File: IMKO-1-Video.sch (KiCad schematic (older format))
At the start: 5 parts, among them U18 82S129, U19 74LS244, U20 74LS244, U26 74LS374

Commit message: Caps, VID lines
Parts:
- added C15, C16: 150nF, symbol C
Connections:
- wire segments 79 -> 80
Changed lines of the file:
@@
-EESchema Schematic File Version 2  date Tue 09 Oct 2012 10:55:53 PM EEST
+EESchema Schematic File Version 2  date Tue 09 Oct 2012 11:59:32 PM EEST
 LIBS:power
 LIBS:device
@@
 LIBS:valves
 LIBS:o_memory
+LIBS:IMKO-1-Video-cache
 EELAYER 27 0
 EELAYER END
@@
 	3200 7100 3500 7100
 Wire Wire Line
-	3200 7200 3900 7200
-Wire Wire Line
-	3900 7200 4450 7200
+	3200 7200 4450 7200
 Wire Wire Line
 	3200 7300 3500 7300
@@
 V.D4
 $Comp
-L GND #PWR?
+L GND #PWR07
 U 1 1 50747FE3
 P 4000 4600
-F 0 "#PWR?" H 4000 4600 30  0001 C CNN
+F 0 "#PWR07" H 4000 4600 30  0001 C CNN
 F 1 "GND" H 4000 4530 30  0001 C CNN
 	1    4000 4600
@@
 	4050 4250 4000 4250
 Wire Wire Line
-	4000 4250 4000 4450
-Wire Wire Line
-	4000 4450 4000 4550
-Wire Wire Line
-	4000 4550 4000 4600
+	4000 4250 4000 4600
 Wire Wire Line
 	4050 4450 4000 4450
@@
 Text Label 3800 4150 0    60   ~ 0
 V.D6
+$Comp
+L C C15
+U 1 1 50748F6B
+P 6200 6600
+F 0 "C15" H 6250 6700 50  0000 L CNN
+F 1 "150nF" H 6250 6500 50  0000 L CNN
+	1    6200 6600
+	1    0    0    -1
+$EndComp
+$Comp
+L GND #PWR08
+U 1 1 50748F84
+P 6200 6850
+F 0 "#PWR08" H 6200 6850 30  0001 C CNN
+F 1 "GND" H 6200 6780 30  0001 C CNN
+	1    6200 6850
+	1    0    0    -1
+$EndComp
+$Comp
+L VCC #PWR09
+U 1 1 50748F8A
+P 6200 6350
+F 0 "#PWR09" H 6200 6450 30  0001 C CNN
+F 1 "VCC" H 6200 6450 30  0000 C CNN
+	1    6200 6350
+	1    0    0    -1
+$EndComp
+Wire Wire Line
+	6200 6350 6200 6400
+Wire Wire Line
+	6200 6800 6200 6850
+$Comp
+L C C16
+U 1 1 50749031
+P 5450 4600
+F 0 "C16" H 5500 4700 50  0000 L CNN
+F 1 "150nF" H 5500 4500 50  0000 L CNN
+	1    5450 4600
+	1    0    0    -1
+$EndComp
+$Comp
+L GND #PWR010
+U 1 1 50749037
+P 5450 4850
+F 0 "#PWR010" H 5450 4850 30  0001 C CNN
+F 1 "GND" H 5450 4780 30  0001 C CNN
+	1    5450 4850
+	1    0    0    -1
+$EndComp
+$Comp
+L VCC #PWR011
+U 1 1 5074903D
+P 5450 4350
+F 0 "#PWR011" H 5450 4450 30  0001 C CNN
+F 1 "VCC" H 5450 4450 30  0000 C CNN
+	1    5450 4350
+	1    0    0    -1
+$EndComp
+Wire Wire Line
+	5450 4350 5450 4400
+Wire Wire Line
+	5450 4800 5450 4850
 $EndSCHEMATC

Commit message: Added U25
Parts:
- added U25: 74LS00, symbol 74LS00
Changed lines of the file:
@@
-EESchema Schematic File Version 2  date Tue 09 Oct 2012 11:59:32 PM EEST
+EESchema Schematic File Version 2  date Wed 10 Oct 2012 12:46:06 AM EEST
 LIBS:power
 LIBS:device
@@
 Wire Wire Line
 	5450 4800 5450 4850
+$Comp
+L 74LS00 U25
+U 1 1 50749ACA
+P 7800 3450
+F 0 "U25" H 7800 3500 60  0000 C CNN
+F 1 "74LS00" H 7800 3350 60  0000 C CNN
+	1    7800 3450
+	1    0    0    -1
+$EndComp
+$Comp
+L 74LS00 U25
+U 2 1 50749AF2
+P 7800 3950
+F 0 "U25" H 7800 4000 60  0000 C CNN
+F 1 "74LS00" H 7800 3850 60  0000 C CNN
+	2    7800 3950
+	1    0    0    -1
+$EndComp
+$Comp
+L 74LS00 U25
+U 3 1 50749B0E
+P 7800 4450
+F 0 "U25" H 7800 4500 60  0000 C CNN
+F 1 "74LS00" H 7800 4350 60  0000 C CNN
+	3    7800 4450
+	1    0    0    -1
+$EndComp
+$Comp
+L 74LS00 U25
+U 4 1 50749B27
+P 7800 4950
+F 0 "U25" H 7800 5000 60  0000 C CNN
+F 1 "74LS00" H 7800 4850 60  0000 C CNN
+	4    7800 4950
+	1    0    0    -1
+$EndComp
 $EndSCHEMATC

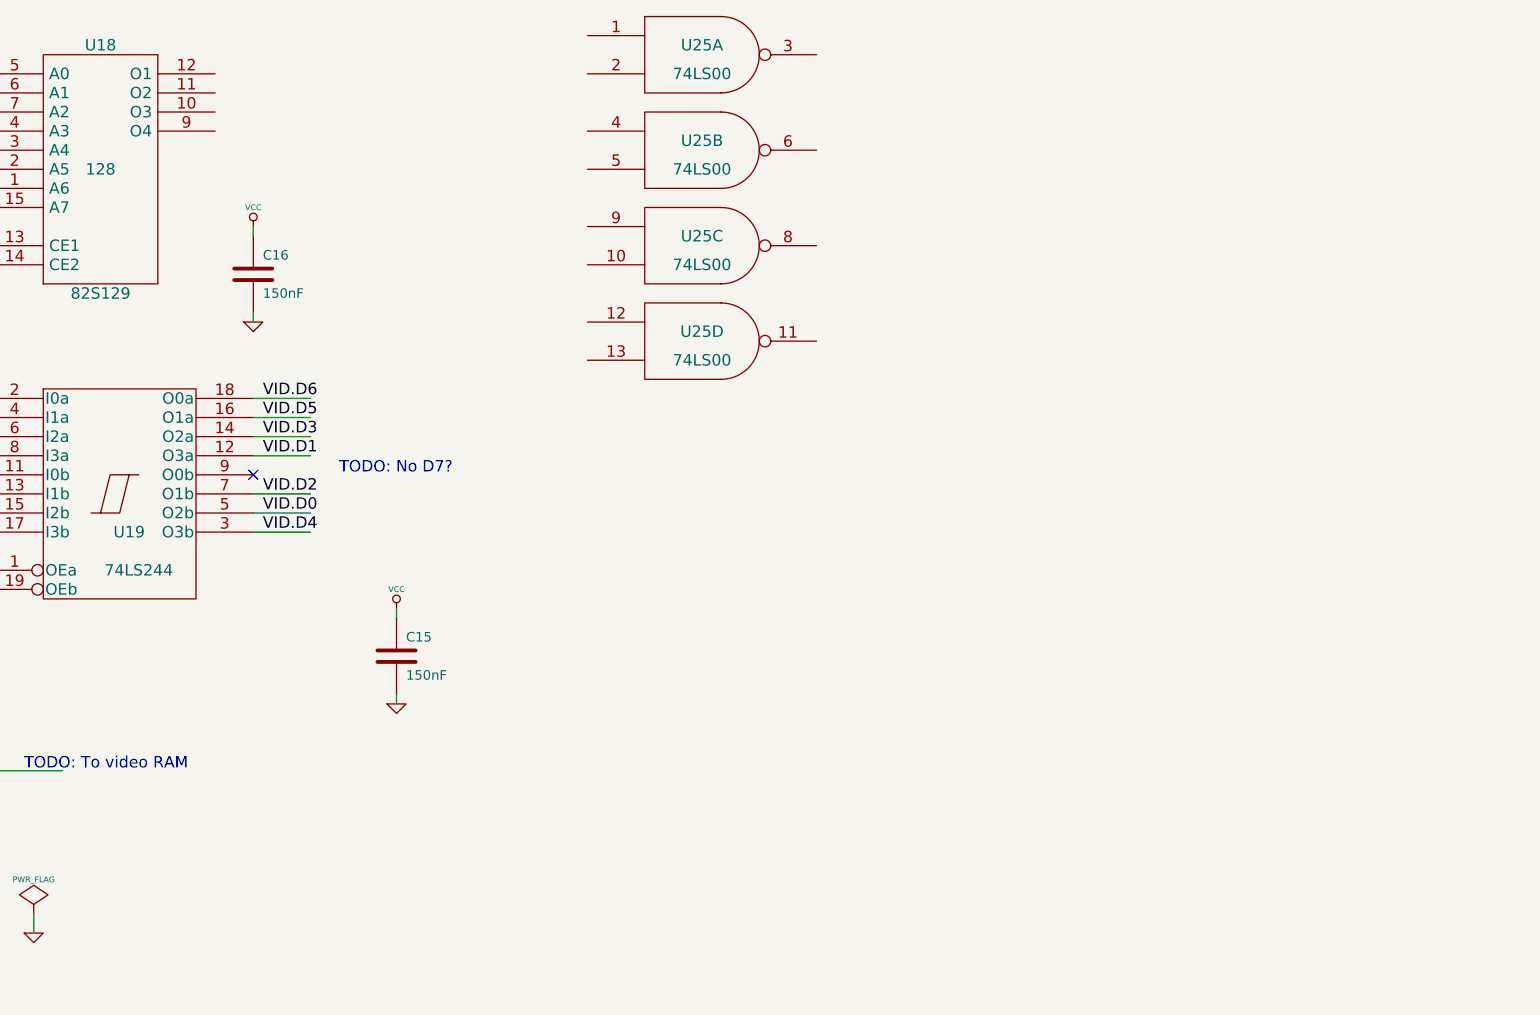
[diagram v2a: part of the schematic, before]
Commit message: Added U23, U24. Fixed caps lib
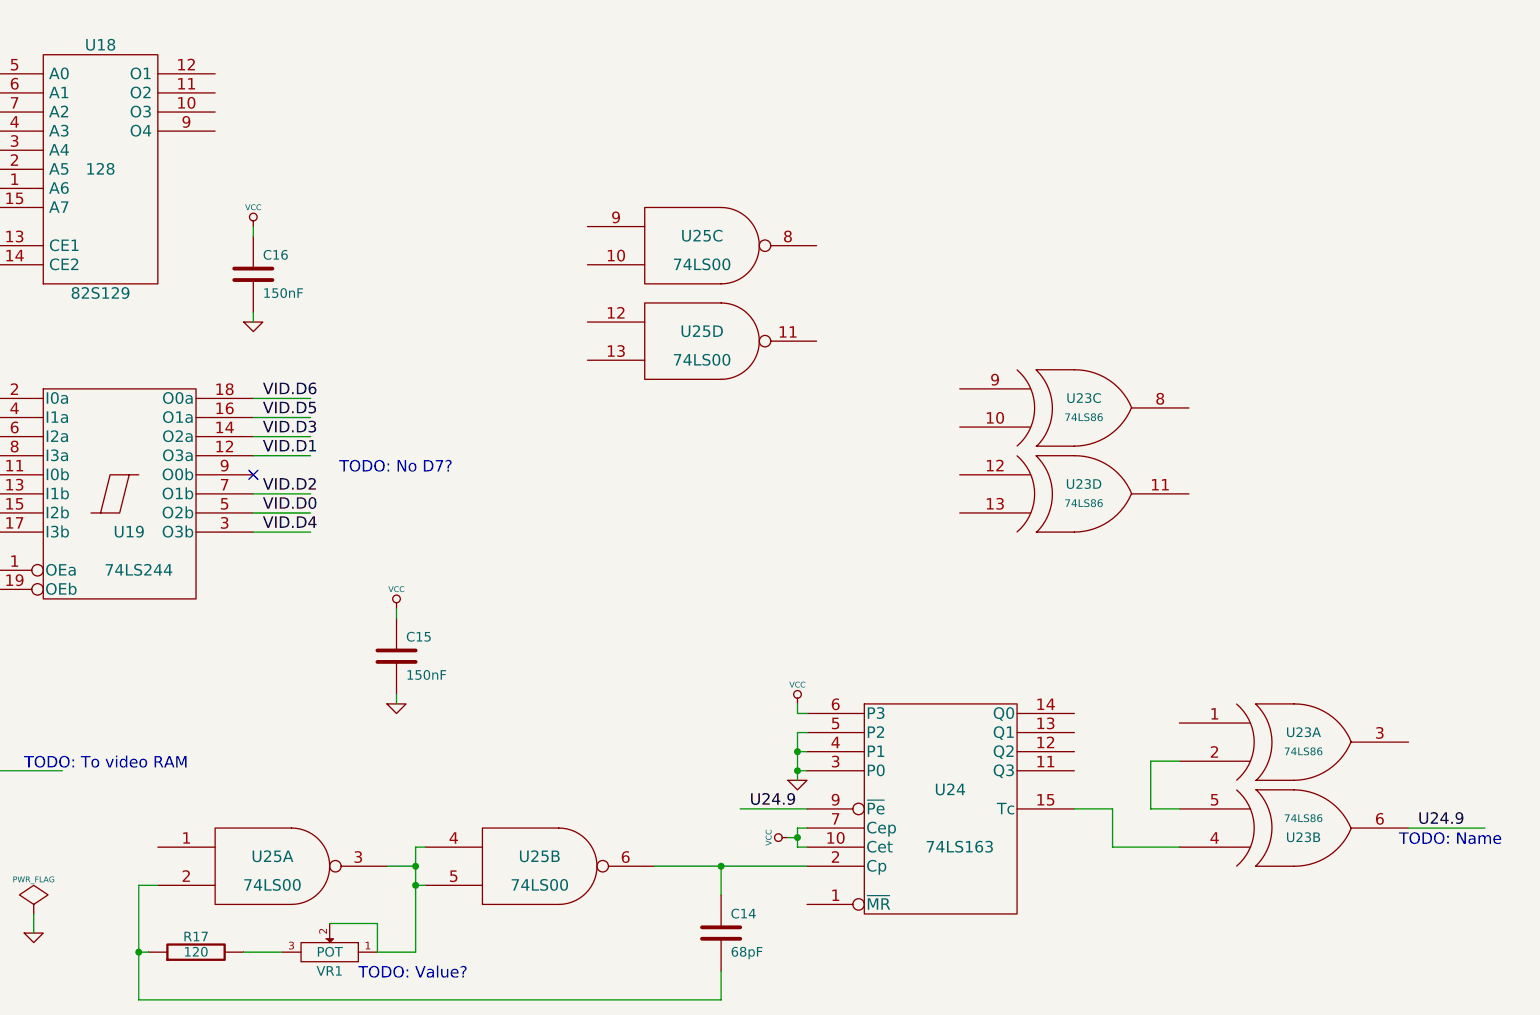
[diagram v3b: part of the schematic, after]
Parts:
- added C14: 68pF, symbol C
- added R17: 120, symbol R
- added U23: 74LS86, symbol 74LS86
- added U24: 74LS163, symbol 74LS163
- added VR1: POT, symbol POT
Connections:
- net labels added: U24.9
- wire segments 80 -> 113
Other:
- note added: "TODO: Name"
- note added: "TODO: Value?"
- moved on the sheet: U25A, U25B
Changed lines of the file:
@@
-EESchema Schematic File Version 2  date Wed 10 Oct 2012 12:46:06 AM EEST
+EESchema Schematic File Version 2  date Wed 10 Oct 2012 09:46:06 PM EEST
 LIBS:power
 LIBS:device
@@
 Sheet 1 1
 Title "noname.sch"
-Date "9 oct 2012"
+Date "10 oct 2012"
 Rev ""
 Comp ""
@@
 L 74LS00 U25
 U 1 1 50749ACA
-P 7800 3450
-F 0 "U25" H 7800 3500 60  0000 C CNN
-F 1 "74LS00" H 7800 3350 60  0000 C CNN
-	1    7800 3450
+P 5550 7700
+F 0 "U25" H 5550 7750 60  0000 C CNN
+F 1 "74LS00" H 5550 7600 60  0000 C CNN
+	1    5550 7700
 	1    0    0    -1
 $EndComp
@@
 L 74LS00 U25
 U 2 1 50749AF2
-P 7800 3950
-F 0 "U25" H 7800 4000 60  0000 C CNN
-F 1 "74LS00" H 7800 3850 60  0000 C CNN
-	2    7800 3950
+P 6950 7700
+F 0 "U25" H 6950 7750 60  0000 C CNN
+F 1 "74LS00" H 6950 7600 60  0000 C CNN
+	2    6950 7700
 	1    0    0    -1
 $EndComp
@@
 	1    0    0    -1
 $EndComp
+$Comp
+L 74LS163 U24
+U 1 1 5075AC5B
+P 9050 7400
+F 0 "U24" H 9100 7500 60  0000 C CNN
+F 1 "74LS163" H 9150 7200 60  0000 C CNN
+	1    9050 7400
+	1    0    0    -1
+$EndComp
+Wire Wire Line
+	8300 7600 8350 7600
+Wire Wire Line
+	8300 7500 8300 7600
+Wire Wire Line
+	8300 7500 8350 7500
+Wire Wire Line
+	8350 6900 8300 6900
+Wire Wire Line
+	8300 6900 8300 6850
+$Comp
+L VCC #PWR012
+U 1 1 5075AE70
+P 8300 6850
+F 0 "#PWR012" H 8300 6950 30  0001 C CNN
+F 1 "VCC" H 8300 6950 30  0000 C CNN
+	1    8300 6850
+	1    0    0    -1
+$EndComp
+$Comp
+L VCC #PWR013
+U 1 1 5075AE76
+P 8250 7550
+F 0 "#PWR013" H 8250 7650 30  0001 C CNN
+F 1 "VCC" H 8250 7650 30  0000 C CNN
+	1    8250 7550
+	0    -1   -1   0
+$EndComp
+Wire Wire Line
+	8250 7550 8300 7550
+Connection ~ 8300 7550
+Wire Wire Line
+	8350 7000 8300 7000
+Wire Wire Line
+	8300 7000 8300 7250
+Wire Wire Line
+	8300 7200 8350 7200
+Wire Wire Line
+	8350 7100 8300 7100
+Connection ~ 8300 7100
+$Comp
+L GND #PWR014
+U 1 1 5075B08E
+P 8300 7250
+F 0 "#PWR014" H 8300 7250 30  0001 C CNN
+F 1 "GND" H 8300 7180 30  0001 C CNN
+	1    8300 7250
+	1    0    0    -1
+$EndComp
+Connection ~ 8300 7200
+Wire Wire Line
+	6350 7600 6300 7600
+Wire Wire Line
+	6300 7600 6300 8150
+Wire Wire Line
+	6300 7800 6350 7800
+Wire Wire Line
+	6300 7700 6150 7700
+Connection ~ 6300 7700
+Wire Wire Line
+	7550 7700 8350 7700
+$Comp
+L C C14
+U 1 1 5075B31A
+P 7900 8050
+F 0 "C14" H 7950 8150 50  0000 L CNN
+F 1 "68pF" H 7950 7950 50  0000 L CNN
+	1    7900 8050
+	1    0    0    -1
+$EndComp
+Wire Wire Line
+	7900 7850 7900 7700
+Connection ~ 7900 7700
+Wire Wire Line
+	4950 7800 4850 7800
+Wire Wire Line
+	4850 7800 4850 8400
+Wire Wire Line
+	4850 8400 7900 8400
+Wire Wire Line
+	7900 8400 7900 8250
+$Comp
+L R R17
+U 1 1 5075B4FB
+P 5150 8150
+F 0 "R17" V 5230 8150 50  0000 C CNN
+F 1 "120" V 5150 8150 50  0000 C CNN
+	1    5150 8150
+	0    -1   -1   0
+$EndComp
+$Comp
+L POT VR1
+U 1 1 5075B50A
+P 5850 8150
+F 0 "VR1" H 5850 8050 50  0000 C CNN
+F 1 "POT" H 5850 8150 50  0000 C CNN
+	1    5850 8150
+	-1   0    0    -1
+$EndComp
+Wire Wire Line
+	5600 8150 5400 8150
+Wire Wire Line
+	4900 8150 4850 8150
+Connection ~ 4850 8150
+Connection ~ 6300 7800
+Wire Wire Line
+	6300 8150 6100 8150
+Text Notes 6000 8300 0    60   ~ 0
+TODO: Value?
+Wire Wire Line
+	5850 8000 6100 8000
+Wire Wire Line
+	6100 8000 6100 8150
+$Comp
+L 74LS86 U23
+U 1 1 5075BBEE
+P 10900 7050
+F 0 "U23" H 10950 7100 50  0000 C CNN
+F 1 "74LS86" H 10950 7000 40  0000 C CNN
+	1    10900 7050
+	1    0    0    -1
+$EndComp
+$Comp
+L 74LS86 U23
+U 2 1 5075BC07
+P 10900 7500
+F 0 "U23" H 10950 7550 50  0000 C CNN
+F 1 "74LS86" H 10950 7450 40  0000 C CNN
+	2    10900 7500
+	1    0    0    1
+$EndComp
+$Comp
+L 74LS86 U23
+U 3 1 5075BC19
+P 9750 5300
+F 0 "U23" H 9800 5350 50  0000 C CNN
+F 1 "74LS86" H 9800 5250 40  0000 C CNN
+	3    9750 5300
+	1    0    0    -1
+$EndComp
+$Comp
+L 74LS86 U23
+U 4 1 5075BC2B
+P 9750 5750
+F 0 "U23" H 9800 5800 50  0000 C CNN
+F 1 "74LS86" H 9800 5700 40  0000 C CNN
+	4    9750 5750
+	1    0    0    -1
+$EndComp
+Wire Wire Line
+	10300 7150 10150 7150
+Wire Wire Line
+	10300 7400 10150 7400
+Wire Wire Line
+	10150 7400 10150 7150
+Wire Wire Line
+	9750 7400 9950 7400
+Wire Wire Line
+	9950 7400 9950 7600
+Wire Wire Line
+	9950 7600 10300 7600
+Wire Wire Line
+	11500 7500 11900 7500
+Text Label 11550 7500 0    60   ~ 0
+U24.9
+Wire Wire Line
+	8350 7400 8000 7400
+Text Label 8050 7400 0    60   ~ 0
+U24.9
+Text Notes 11450 7600 0    60   ~ 0
+TODO: Name
 $EndSCHEMATC
